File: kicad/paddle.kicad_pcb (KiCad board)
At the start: 4 copper layers, 76.7 x 51.3 mm, 138 parts, among them J101 CONN_02X05, J301 Battery, M101 MICROSD, P201 100k, P401 100k, P501 100k, P601 100k, Q301 DMG3414U, Q302 DMG3415U, Q303 DMG3415U, Q601 MMBT4401, Q602 MMBT4401, SW301 SW_DPDT_x2, U101 OPA333, U102 BME280, U103 ESP32-WROOM, U104 FGPMMOPA6H GPS, U107 DNP TLVH431, U201 INA333, U202 ADS1115, U301 MCP73831/2, U302 NCP694-3.3, U401 INA333, U402 ADS1115, U501 INA333, U502 ADS1115, U601 INA333, U602 ADS1115, U603 USB_B_Socket, U605 CP2104, U701 NCP694-3.3

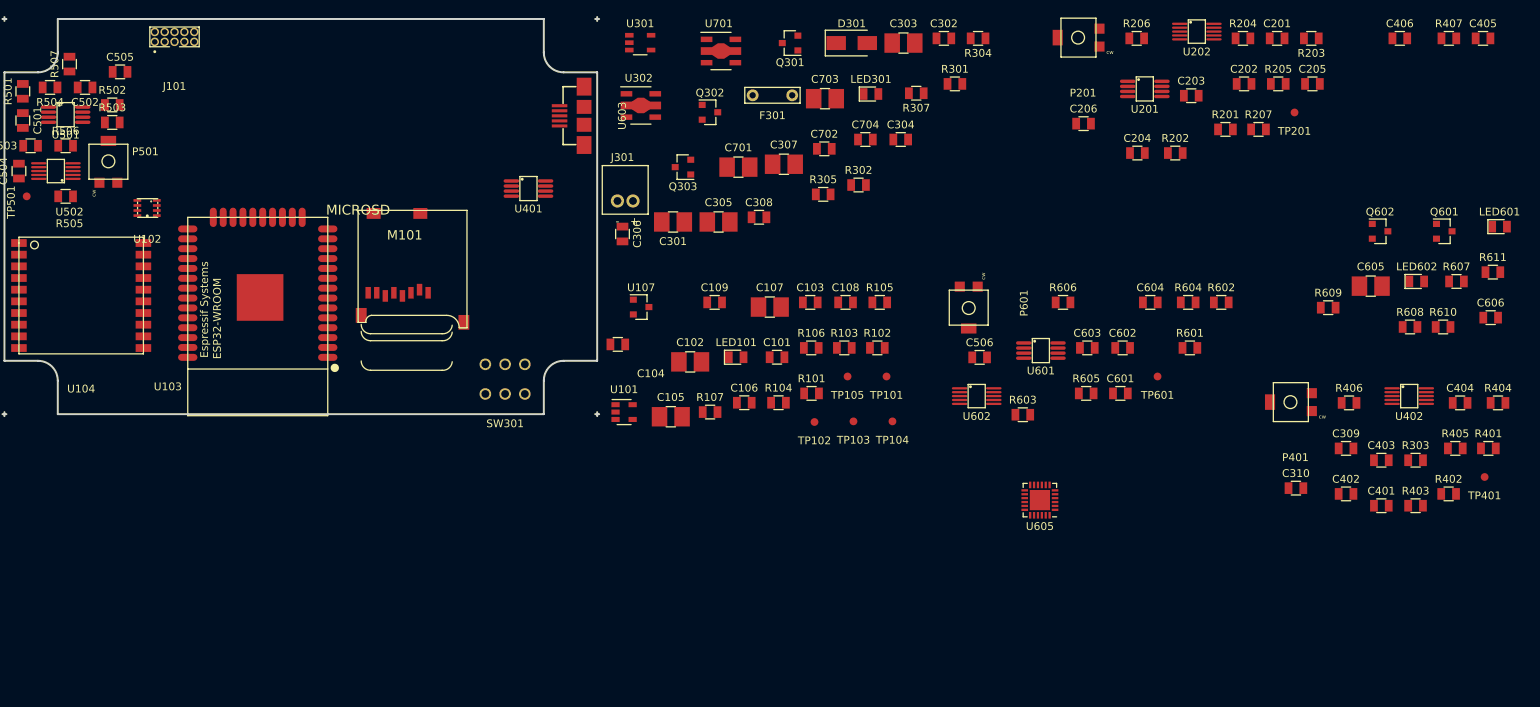
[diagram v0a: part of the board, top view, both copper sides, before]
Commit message: Add LEDs to schematic, add pullup to ALERT0, remove ALERT 1-3
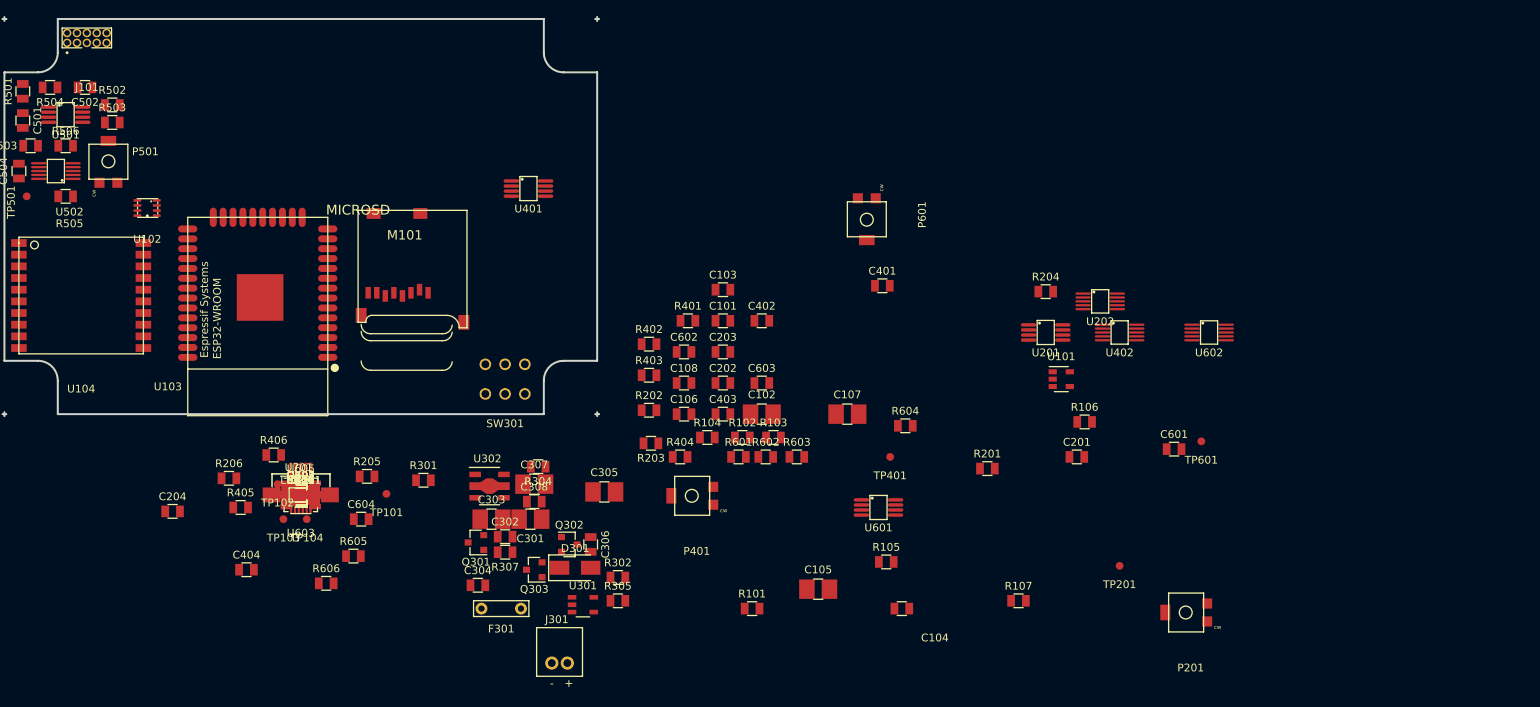
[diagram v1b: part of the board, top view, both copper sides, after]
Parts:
- removed LED101, LED601, LED602: LED, paddle:SMD_D_0805
- removed R607: 1k, paddle:SMD_0805
- removed R608, R609: R_US, paddle:SMD_0805
- removed TP105: SCK, paddle:tp_th_1mm
- TP101: value VREF -> AN1
- moved C405 162.9 mm to (114.2, 129.4)
- moved R407 158.8 mm to (114.2, 129.4)
- moved C404 157.5 mm to (107.2, 139.0)
- moved R405 156.3 mm to (106.5, 131.0)
- moved R611 155.9 mm to (114.2, 129.4)
- moved C606 154.7 mm to (114.2, 129.4)
- moved C406 153.0 mm to (114.2, 129.4)
- moved Q601 150.9 mm to (114.2, 129.4)
- moved R610 148.4 mm to (114.2, 129.4)
- moved R303 143.4 mm to (114.2, 129.4)
- moved Q602 142.8 mm to (114.2, 129.4)
- moved C205 140.4 mm to (114.2, 129.4)
- moved C605 140.1 mm to (114.2, 129.4)
- moved R406 138.4 mm to (110.8, 124.2)
- moved C309 134.5 mm to (114.2, 129.4)
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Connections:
- R107 pad 1: Net-(LED101-PadA) -> (no net)
- U605 pad 13: Net-(R609-Pad1) -> (no net)
- U605 pad 14: Net-(R608-Pad1) -> (no net)
- U605 pad 25: GND -> Net-(U605-Pad25)
- U605 pad 9: Net-(R607-Pad1) -> (no net)

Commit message: layout sample analog a/d section, add buttons, battery but not footprints
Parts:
- removed C104: 1.0uF, paddle:SMD_0805
- removed C105, C107, C303, C305, C307, C605: 10uF, paddle:SMD_1206
- removed C106, C108, C304, C306, C308, C309, C501, C502, C503, C505, C603, C606, C704: 0.1uF, paddle:SMD_0805
- removed C109, C310, C506: DNP 0.1uF, paddle:SMD_0805
- removed C504, C604: 0.22uF, paddle:SMD_0805
- removed D301: Schottky, paddle:D_SMA
- removed F301: 1A Poly, paddle:radial-0.2-in-0.7mm-hole
- removed J101: CONN_02X05, paddle:header-0.050-10-pin-through-hole
- removed J301: Battery, paddle:JST_battery_header_B2B-PH-K-S
- removed M101: MICROSD, adafruit:MICROSD
- removed P401, P501, P601: 100k, paddle:TT_model_23_pot_smd_4mm
- removed Q303: DMG3415U, paddle:SOT-23
- removed Q601, Q602: MMBT4401, paddle:SOT-23
- removed R307: 1.0Meg, paddle:SMD_0805
- removed R604: 250, paddle:SMD_0805
- removed R605: 0, paddle:SMD_0805
- removed R606: DNP 100k, paddle:SMD_0805
- removed R610, R611: 10k, paddle:SMD_0805
- removed SW301: SW_DPDT_x2, paddle:dpdt_switch
- removed TP101, TP401, TP501: AN1, paddle:tp_th_1mm
- removed TP102: GND, paddle:tp_th_1mm
- removed TP103: SDA, paddle:tp_th_1mm
- removed TP104: SCK, paddle:tp_th_1mm
- removed U103: ESP32-WROOM, paddle:ESP32-WROOM
- removed U104: FGPMMOPA6H GPS, paddle:FGPMMOPA6H
- removed U107: DNP TLVH431, paddle:SOT-23
- removed U603: USB_B_Socket, paddle:USB_micro_B_FCI_10104110
- removed U605: CP2104, paddle:QFN-24-1EP_4x4mm_Pitch0.5mm
- added C1001: 0.01uF, paddle:SMD_0805, F.Cu at (313.5, 51.1)
- added C1002: 0.01uF, paddle:SMD_0805, F.Cu at (319.3, 45.3)
- added C1003: DNP 0.01uF, paddle:SMD_0805, F.Cu at (288.0, 50.4)
- added C1004: 0.1uF, paddle:SMD_0805, F.Cu at (321.1, 39.4)
- added C1005: 0.01uF, paddle:SMD_0805, F.Cu at (313.8, 45.3)
- added C1006: 0.22uF, paddle:SMD_0805, F.Cu at (308.0, 51.1)
- added C1101: 10uF, paddle:SMD_1206, F.Cu at (219.8, 148.7)
- added C1102: 0.1uF, paddle:SMD_0805, F.Cu at (227.9, 141.0)
- added C407: 0.1uF, paddle:SMD_0805, F.Cu at (183.4, 96.6)
- added C408: 0.1uF, paddle:SMD_0805, F.Cu at (195.3, 82.4)
- added C409: 10uF, paddle:SMD_1206, F.Cu at (183.5, 78.4)
- added C410: 10uF, paddle:SMD_1206, F.Cu at (189.4, 78.4)
- added C411: 0.1uF, paddle:SMD_0805, F.Cu at (201.2, 76.5)
- added C412: 0.1uF, paddle:SMD_0805, F.Cu at (190.8, 84.9)
- added C801: 0.01uF, paddle:SMD_0805, F.Cu at (164.8, 154.2)
- added C802: 0.01uF, paddle:SMD_0805, F.Cu at (185.4, 141.0)
- added C803: DNP 0.01uF, paddle:SMD_0805, F.Cu at (157.4, 152.0)
- added C804: 0.1uF, paddle:SMD_0805, F.Cu at (169.8, 154.2)
- added C805: 0.01uF, paddle:SMD_0805, F.Cu at (177.7, 148.4)
- added C806: 0.22uF, paddle:SMD_0805, F.Cu at (172.2, 148.4)
- added C901: 0.01uF, paddle:SMD_0805, F.Cu at (231.0, 114.0)
- added C902: 0.01uF, paddle:SMD_0805, F.Cu at (223.6, 119.8)
- added C903: DNP 0.01uF, paddle:SMD_0805, F.Cu at (216.2, 117.6)
- added C904: 0.1uF, paddle:SMD_0805, F.Cu at (236.0, 114.0)
- added C905: 0.01uF, paddle:SMD_0805, F.Cu at (229.1, 119.8)
- added C906: 0.22uF, paddle:SMD_0805, F.Cu at (244.2, 106.6)
- added D401: Schottky, paddle:D_SMA, F.Cu at (185.1, 71.3)
- added F401: 1A Poly, paddle:radial-0.2-in-0.7mm-hole, F.Cu at (176.8, 76.2)
- added J401: Battery, paddle:JST_battery_header_B2B-PH-K-S, F.Cu at (155.9, 76.8)
- added J501: CONN_02X05, paddle:header-0.050-10-pin-through-hole, F.Cu at (337.8, 68.6)
- added L701: bead, paddle:SMD_0805, F.Cu at (35.4, 106.8)
- added LED101: LED, paddle:SMD_D_0805, F.Cu at (181.0, 120.3)
- added LED102: LED, paddle:SMD_D_0805, F.Cu at (186.9, 106.6)
- added LED103: LED, paddle:SMD_D_0805, F.Cu at (187.3, 112.5)
- added LED104: LED, paddle:SMD_D_0805, F.Cu at (192.8, 106.6)
- added LED401: Charge, paddle:SMD_D_0805, F.Cu at (181.0, 84.9)
- added LED701: LED, paddle:SMD_D_0805, F.Cu at (30.4, 108.0)
- added M1101: MICROSD, adafruit:MICROSD, F.Cu at (131.1, 94.3)
- added P1001: 100k, paddle:TT_model_23_pot_smd_4mm, F.Cu at (286.8, 39.3)
- added P801: 100k, paddle:TT_model_23_pot_smd_4mm, F.Cu at (156.2, 140.9)
- added P901: 100k, paddle:TT_model_23_pot_smd_4mm, F.Cu at (215.0, 106.5)
- added Q1101: DMG3415U, paddle:SOT-23, F.Cu at (221.1, 141.6)
- added Q401: DMG3414U, paddle:SOT-23, F.Cu at (177.1, 71.3)
- added Q402: DMG3415U, paddle:SOT-23, F.Cu at (156.9, 97.1)
- added Q403: DMG3415U, paddle:SOT-23, F.Cu at (166.8, 89.8)
- added Q701: DMG3415U, paddle:SOT-23, F.Cu at (31.6, 94.5)
- added R1001: 10k 0.1%, paddle:SMD_0805, F.Cu at (287.0, 56.3)
- added R1002: 20k 0.1%, paddle:SMD_0805, F.Cu at (309.6, 39.4)
- added R1003: 1.0M, paddle:SMD_0805, F.Cu at (302.6, 46.8)
- added R1004: 250, paddle:SMD_0805, F.Cu at (308.5, 45.3)
- added R1005: 0, paddle:SMD_0805, F.Cu at (315.9, 39.4)
- added R1006: 10k, paddle:SMD_0805, F.Cu at (302.6, 52.7)
- added R1007: DNP 100k, paddle:SMD_0805, F.Cu at (294.3, 39.4)
- added R108: 330, paddle:SMD_0805, F.Cu at (192.4, 112.5)
- added R1101: 1MEG, paddle:SMD_0805, F.Cu at (219.5, 155.1)
- added R508: 10k 0.1%, paddle:R_0805, F.Cu at (348.7, 77.9)
- added R701: 1MEG, paddle:SMD_0805, F.Cu at (35.4, 101.0)
- added R702: 330, paddle:SMD_0805, F.Cu at (44.0, 99.8)
- added R703: 330, paddle:SMD_0805, F.Cu at (39.7, 101.0)
- added R704: 330, paddle:SMD_0805, F.Cu at (43.7, 93.9)
- added R801: 10k 0.1%, paddle:SMD_0805, F.Cu at (165.7, 148.4)
- added R802: 20k 0.1%, paddle:SMD_0805, F.Cu at (156.4, 157.8)
- added R803: 1.0M, paddle:SMD_0805, F.Cu at (174.2, 154.2)
- added R804: 250, paddle:SMD_0805, F.Cu at (182.5, 148.4)
- added R805: 0, paddle:SMD_0805, F.Cu at (190.3, 141.0)
- added R806: 10k, paddle:SMD_0805, F.Cu at (178.4, 154.2)
- added R807: DNP 100k, paddle:SMD_0805, F.Cu at (163.7, 141.0)
- added R901: 10k 0.1%, paddle:SMD_0805, F.Cu at (224.5, 114.0)
- added R902: 20k 0.1%, paddle:SMD_0805, F.Cu at (215.2, 123.4)
- added R903: 1.0M, paddle:SMD_0805, F.Cu at (244.7, 112.5)
- added R904: 250, paddle:SMD_0805, F.Cu at (249.1, 106.6)
- added R905: 0, paddle:SMD_0805, F.Cu at (240.4, 114.0)
- added R906: 10k, paddle:SMD_0805, F.Cu at (234.0, 119.8)
- added R907: DNP 100k, paddle:SMD_0805, F.Cu at (222.6, 106.6)
- added SW401: SW_DPDT_x2, paddle:dpdt_switch, F.Cu at (167.4, 79.6)
- added TP1001: AN1, paddle:tp_th_1mm, F.Cu at (295.6, 52.0)
- added TP301: RXD, paddle:tp_th_1mm, F.Cu at (328.8, 142.5)
- added TP302: TXD, paddle:tp_th_1mm, F.Cu at (322.8, 143.7)
- added TP801: AN1, paddle:tp_th_1mm, F.Cu at (187.2, 144.7)
- added TP901: AN1, paddle:tp_th_1mm, F.Cu at (238.6, 117.6)
- added U1001: INA333, paddle:S-PDSO-G8, F.Cu at (296.3, 45.9)
- added U1002: ADS1115, paddle:VSSOP10-S-PDSO-G10, F.Cu at (302.1, 38.6)
- added U303: CP2104, paddle:QFN-24-1EP_4x4mm_Pitch0.5mm, F.Cu at (308.2, 134.5)
- added U403: NCP694-3.3, paddle:SOT89-5, F.Cu at (168.3, 72.3)
- added U801: INA333, paddle:S-PDSO-G8, F.Cu at (179.0, 140.1)
- added U802: ADS1115, paddle:VSSOP10-S-PDSO-G10, F.Cu at (171.5, 140.1)
- added U901: INA333, paddle:S-PDSO-G8, F.Cu at (237.8, 105.7)
- added U902: ADS1115, paddle:VSSOP10-S-PDSO-G10, F.Cu at (230.3, 105.7)
- C101: value 0.1uF -> 1.0uF
- C201, C202, C205, C702: value 0.1uF -> 0.01uF
- C203: value 0.1uF -> DNP 0.01uF
- C204, C404: value 0.22uF -> 0.1uF
- C206: value DNP 0.1uF -> 0.22uF
- C401, C403, C405: value 0.1uF -> 10uF; footprint paddle:SMD_0805 -> paddle:SMD_1206
- C406: value DNP 0.1uF -> 10uF; footprint paddle:SMD_0805 -> paddle:SMD_1206
- C601: value 0.1uF -> DNP 0.1uF
- C703: value 10uF -> 1uF
- LED301: value Charge -> LED
- Q301: value DMG3414U -> MMBT4401
- Q302: value DMG3415U -> MMBT4401
- R102: value 0 -> 4.7k
- R104: value 4.7k -> 10k
- R105, R106: value 10k -> 330
- R107: value R_US -> 330
- R201: value 47k -> 10k 0.1%
- R202: value 47K -> 20k 0.1%
- R206: value DNP 100k -> 10k
- R207: value 47K -> DNP 100k
- R301: value 1.0K -> 1k
- R302: value 4.7K -> R_US
- R303: value 47K -> R_US
- R304, R305: value 1Meg -> 10k
- R401: value 47k -> 1.0K
- R402: value 47K -> 1Meg
- R403: value 1.0M -> 1Meg
- R404: value 250 -> 4.7K
- R405: value 0 -> 1.0Meg
- R406: value DNP 100k -> 100k
- R407: value 47K -> 100k
- R501: value 47k -> 10k 0.1%; footprint paddle:SMD_0805 -> paddle:R_0805
- R502, R507: value 47K -> 10k 0.1%; footprint paddle:SMD_0805 -> paddle:R_0805
- R503: value 1.0M -> 10k 0.1%; footprint paddle:SMD_0805 -> paddle:R_0805
- R504: value 250 -> 10k 0.1%; footprint paddle:SMD_0805 -> paddle:R_0805
- R505: value 0 -> 10k 0.1%; footprint paddle:SMD_0805 -> paddle:R_0805
- R506: value DNP 100k -> 10k 0.1%; footprint paddle:SMD_0805 -> paddle:R_0805
- R601: value 47k -> 10k
- R602: value 47K -> 0
- R603: value 1.0M -> 10k
- U101: value OPA333 -> BME280; footprint paddle:sot23-5 -> paddle:BME280
- U102: value BME280 -> ESP32-WROOM; footprint paddle:BME280 -> paddle:ESP32-WROOM
- U301: value MCP73831/2 -> USB_B_Socket; footprint paddle:SOT-23-5 -> paddle:USB_micro_B_FCI_10104110
- U302: value NCP694-3.3 -> SP3003-04
- U401: value INA333 -> MCP73831/2; footprint paddle:S-PDSO-G8 -> paddle:SOT-23-5
- U402: value ADS1115 -> NCP694-3.3; footprint paddle:VSSOP10-S-PDSO-G10 -> paddle:SOT89-5
- U501: value INA333 -> SP3003-04
- U502: value ADS1115 -> SP3003-04
- U601: value INA333 -> DNP TLVH431; footprint paddle:S-PDSO-G8 -> paddle:SOT-23
- U602: value ADS1115 -> OPA333; footprint paddle:VSSOP10-S-PDSO-G10 -> paddle:sot23-5
- U701: value NCP694-3.3 -> FGPMMOPA6H GPS; footprint paddle:SOT89-5 -> paddle:FGPMMOPA6H
- moved R501 270.7 mm to (349.0, 69.0)
- moved R506 264.9 mm to (348.7, 73.2)
- moved R505 261.4 mm to (344.8, 74.0)
- moved R503 255.1 mm to (344.8, 69.3)
- moved U501 253.5 mm to (337.5, 78.0)
- moved R504 247.4 mm to (329.3, 81.0)
- moved U502 245.9 mm to (328.2, 72.3)
- moved R502 235.5 mm to (325.5, 80.9)
- moved R507 235.3 mm to (344.1, 78.7)
- moved R303 204.6 mm to (318.2, 145.9)
- moved LED301 200.8 mm to (314.8, 140.1)
- moved R301 194.5 mm to (324.1, 140.1)
- moved C302 188.1 mm to (328.5, 138.9)
- moved C301 178.7 mm to (322.5, 133.6)
- moved Q301 178.7 mm to (315.4, 133.6)
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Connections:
- C101 pad 1: +3.3VA -> /RESET*
- C202 pad 1: +3.3VA -> Net-(C202-Pad1)
- C203 pad 1: Net-(C203-Pad1) -> Net-(C202-Pad1)
- C203 pad 2: GND -> Net-(C201-Pad1)
- C206 pad 1: Net-(C205-Pad1) -> +3.3VA
- C206 pad 2: Net-(C201-Pad1) -> GND
- C301 pad 1: /Power/+VBUS -> +3V3
- C302 pad 1: /Power/+VBUS -> +3V3
- C401 pad 1: Net-(C310-Pad2) -> /Power/+VBUS
- C402 pad 1: +3.3VA -> /Power/+VBUS
- C403 pad 1: Net-(C403-Pad1) -> /Power/V_BAT
- C404 pad 1: +3.3VA -> /Power/V_BAT
- C405 pad 1: Net-(C405-Pad1) -> /Power/V_UNREG_SW
- C406 pad 1: Net-(C405-Pad1) -> /Power/V_UNREG_SW
- C406 pad 2: Net-(C406-Pad2) -> GND
- C601 pad 1: Net-(C506-Pad2) -> Net-(C601-Pad1)
- C701 pad 1: /Power/V_UNREG_SW -> Net-(C701-Pad1)
- C702 pad 1: /Power/V_UNREG_SW -> Net-(C701-Pad1)
- C703 pad 1: +3.3VA -> Net-(BT701-Pad1)
- LED301 pad K: Net-(LED301-PadK) -> GND
- Q301 pad 1: /KEEPALIVE -> Net-(Q301-Pad1)
- Q301 pad 2: GND -> Net-(Q301-Pad2)
- Q301 pad 3: Net-(Q301-Pad3) -> (no net)
- Q302 pad 1: Net-(Q301-Pad3) -> Net-(Q302-Pad1)
- Q302 pad 2: /Power/V_UNREG -> Net-(Q302-Pad2)
- Q302 pad 3: /Power/V_UNREG_SW -> /BOOTLOAD*
- R101 pad 1: Net-(C109-Pad1) -> +3V3
- R101 pad 2: Net-(R101-Pad2) -> /ALERT0
- R102 pad 1: Net-(R101-Pad2) -> +3V3
- R102 pad 2: GND -> /SCK
- R103 pad 2: /SCK -> /SDA
- R104 pad 2: /SDA -> /RESET*
- R105 pad 1: +3V3 -> /LEDG
- R105 pad 2: /RESET* -> Net-(LED101-PadA)
- R106 pad 1: +3.3VA -> /LEDR
- R106 pad 2: Net-(C109-Pad1) -> Net-(LED102-PadA)
- R107 pad 1: (no net) -> /LEDY
- R202 pad 1: Net-(C205-Pad1) -> Net-(C202-Pad1)
- R203 pad 1: Net-(C205-Pad1) -> Net-(C202-Pad1)
- R206 pad 1: GND -> Net-(C205-Pad1)
- R206 pad 2: Net-(C203-Pad1) -> /AUX_IN_0
- R207 pad 1: Net-(C203-Pad1) -> GND
- R207 pad 2: /AUX_IN_0 -> Net-(C205-Pad1)
- R301 pad 1: /Power/+VBUS -> Net-(R301-Pad1)
- R301 pad 2: Net-(LED301-PadA) -> +3V3
- R302 pad 1: GND -> Net-(R302-Pad1)
- R302 pad 2: Net-(R302-Pad2) -> Net-(LED301-PadA)
- R303 pad 1: Net-(C403-Pad1) -> Net-(R303-Pad1)
- R303 pad 2: /AUX_IN_1 -> (no net)
- R304 pad 1: GND -> Net-(Q301-Pad1)
- R304 pad 2: /KEEPALIVE -> Net-(Q302-Pad2)
- R305 pad 1: Net-(Q301-Pad3) -> Net-(Q302-Pad1)
- R305 pad 2: /Power/V_UNREG -> Net-(Q301-Pad2)
- R401 pad 1: Net-(C310-Pad2) -> /Power/+VBUS
- R401 pad 2: /IN_1 -> Net-(LED401-PadA)
- R402 pad 1: Net-(C309-Pad1) -> GND
- R402 pad 2: /VREF -> /KEEPALIVE
- R403 pad 1: Net-(C309-Pad1) -> Net-(Q401-Pad3)
- R403 pad 2: Net-(P401-Pad2) -> /Power/V_UNREG
- R404 pad 1: Net-(R404-Pad1) -> GND
- R405 pad 2: Net-(R405-Pad2) -> /Power/+VBUS
- R406 pad 2: Net-(C403-Pad1) -> /+3.3VA_ENABLE
- R407 pad 1: Net-(C503-Pad1) -> /SHUTDOWN*
- R407 pad 2: /AUX_IN_2 -> +3V3
- R501 pad 1: Net-(C406-Pad2) -> /AUX_IN_0
- R501 pad 2: /IN_2 -> Net-(J501-Pad3)
- R502 pad 1: Net-(C405-Pad1) -> /AUX_IN_1
- R502 pad 2: /VREF -> Net-(J501-Pad5)
- R503 pad 1: Net-(C405-Pad1) -> /AUX_IN_2
- R504 pad 1: Net-(R504-Pad1) -> /AUX_IN_3
- R504 pad 2: Net-(R504-Pad2) -> Net-(J501-Pad9)
- R505 pad 1: GND -> Net-(J501-Pad2)
- R505 pad 2: Net-(R505-Pad2) -> /IN_0
- R506 pad 1: GND -> Net-(J501-Pad4)
- R506 pad 2: Net-(C503-Pad1) -> /IN_1
- R507 pad 1: Net-(C603-Pad1) -> Net-(J501-Pad6)
- R507 pad 2: /AUX_IN_3 -> /IN_2
- R601 pad 1: Net-(C506-Pad2) -> Net-(C601-Pad1)
- R601 pad 2: /IN_3 -> Net-(R601-Pad2)
- R602 pad 1: Net-(C505-Pad1) -> Net-(R601-Pad2)
- R602 pad 2: /VREF -> GND
- R603 pad 1: Net-(C505-Pad1) -> +3.3VA
- R603 pad 2: Net-(P601-Pad2) -> Net-(C601-Pad1)
- TP601 pad 1: Net-(TP601-Pad1) -> /VREF
- U101 pad 1: /VREF -> GND
- U101 pad 2: GND -> +3V3
- U101 pad 3: Net-(C109-Pad1) -> /SDA
- U101 pad 4: /VREF -> /SCK
- U101 pad 5: +3.3VA -> GND
- U102 pad 3: /SDA -> /RESET*
- U102 pad 4: /SCK -> (no net)
- U102 pad 5: GND -> (no net)
- U102 pad 6: +3V3 -> /ALERT0
- U102 pad 7: GND -> /SHUTDOWN*
- U102 pad 8: +3V3 -> /+3.3VA_ENABLE
- U201 pad 2: Net-(C205-Pad1) -> Net-(C202-Pad1)
- U202 pad 4: Net-(C203-Pad1) -> Net-(C205-Pad1)
- U301 pad 1: Net-(LED301-PadK) -> /Power/+VBUS
- U301 pad 2: GND -> Net-(U301-Pad2)
- U301 pad 3: /Power/V_BAT -> Net-(U301-Pad3)
- U301 pad 4: /Power/+VBUS -> (no net)
- U301 pad 5: Net-(R302-Pad2) -> GND
- U302 pad 3: /Power/V_UNREG_SW -> Net-(U301-Pad3)
- U302 pad 4: /Power/V_UNREG_SW -> Net-(U301-Pad2)
- U401 pad 1: Net-(R404-Pad1) -> Net-(LED401-PadK)
- U401 pad 2: Net-(C309-Pad1) -> GND
- U401 pad 3: Net-(C310-Pad2) -> /Power/V_BAT
- U401 pad 4: Net-(R405-Pad2) -> /Power/+VBUS
- U401 pad 5: /VREF -> Net-(R404-Pad2)
- U402 pad 1: +3V3 -> (no net)
- U402 pad 2: /ALERT1 -> GND
- U402 pad 3: GND -> /Power/V_UNREG_SW
- U402 pad 4: Net-(C403-Pad1) -> /Power/V_UNREG_SW
- U402 pad 5: Net-(TP401-Pad1) -> +3V3
- U501 pad 1: Net-(R504-Pad1) -> /AUX_IN_3
- U501 pad 2: Net-(C405-Pad1) -> GND
- U501 pad 3: Net-(C406-Pad2) -> /AUX_IN_2
- U501 pad 4: Net-(R505-Pad2) -> /AUX_IN_1
- U501 pad 5: /VREF -> +3V3
- U501 pad 6: Net-(U501-Pad6) -> /AUX_IN_0
- U501 pad 7: +3.3VA -> (no net)
- U501 pad 8: Net-(R504-Pad2) -> (no net)
- U502 pad 1: /SDA -> /IN_3
- U502 pad 10: /SCK -> (no net)
- U502 pad 2: /ALERT2 -> GND
- U502 pad 3: GND -> /IN_2
- U502 pad 4: Net-(C503-Pad1) -> /IN_1
- U502 pad 5: Net-(TP501-Pad1) -> +3V3
- U502 pad 6: Net-(U501-Pad6) -> /IN_0
- U502 pad 7: /VREF -> (no net)
- U502 pad 8: +3.3VA -> (no net)
- U502 pad 9: /SDA -> (no net)
- U601 pad 1: Net-(R604-Pad1) -> Net-(R601-Pad2)
- U601 pad 2: Net-(C505-Pad1) -> Net-(C601-Pad1)
- U601 pad 3: Net-(C506-Pad2) -> GND
- U602 pad 1: /SCK -> /VREF
- U602 pad 2: /ALERT3 -> GND
- U602 pad 3: GND -> Net-(C601-Pad1)
- U602 pad 4: Net-(C603-Pad1) -> /VREF
- U602 pad 5: Net-(TP601-Pad1) -> +3.3VA
- U701 pad 1: (no net) -> Net-(C701-Pad1)
- U701 pad 2: GND -> /GPS_RESET*
- U701 pad 3: /Power/V_UNREG_SW -> GND
- U701 pad 4: /Power/V_UNREG_SW -> Net-(BT701-Pad1)
- U701 pad 5: +3.3VA -> Net-(R704-Pad2)
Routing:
- net /VREF: track 0.00 -> 30.5 mm
- net Net-(C202-Pad1): track 0.00 -> 22.4 mm, vias 0 -> 2
- net GND: track 0.00 -> 11.7 mm, vias 0 -> 6
- net Net-(C205-Pad1): track 0.00 -> 11.0 mm
- net Net-(C201-Pad1): track 0.00 -> 10.5 mm
- net Net-(U201-Pad6): track 0.00 -> 8.29 mm, vias 0 -> 2
- net Net-(R205-Pad2): track 0.00 -> 7.11 mm
- net Net-(R204-Pad2): track 0.00 -> 4.91 mm, vias 0 -> 2
- net +3.3VA: track 0.00 -> 4.36 mm, vias 0 -> 2
- net Net-(P201-Pad2): track 0.00 -> 2.60 mm
- net Net-(R204-Pad1): track 0.00 -> 2.13 mm
- added copper zone on In2.Cu, net +3.3VA
- removed copper zone on In2.Cu, net +3V3
